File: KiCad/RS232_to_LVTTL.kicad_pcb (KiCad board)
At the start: 2 copper layers, 36.1 x 34 mm, 1 part, among them J1 DB25_Female

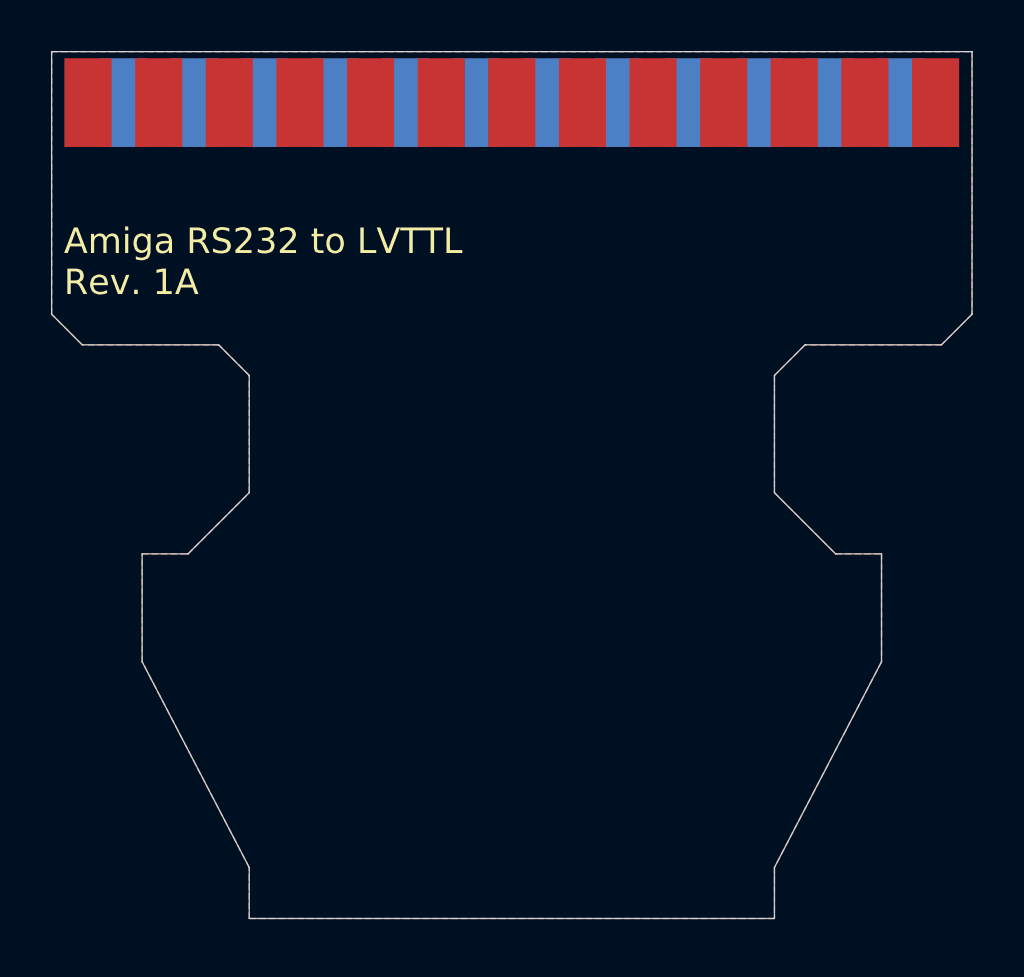
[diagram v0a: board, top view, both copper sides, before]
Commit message: Added power circuit convert 12V to 3.3V
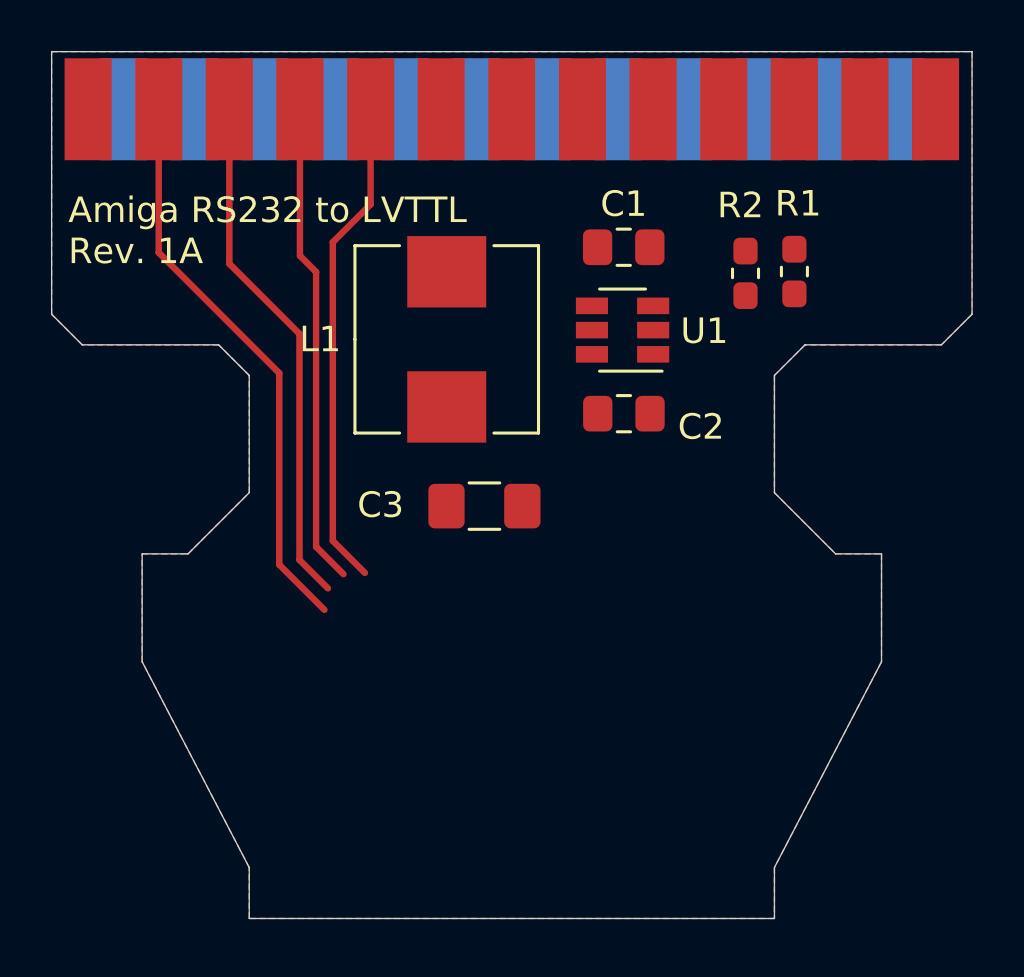
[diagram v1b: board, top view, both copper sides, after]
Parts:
- added C1: 10uF, Capacitor_SMD:C_0805_2012Metric_Pad1.15x1.40mm_HandSolder, F.Cu at (110.9, 57.7)
- added C2: 100nF, Capacitor_SMD:C_0805_2012Metric_Pad1.15x1.40mm_HandSolder, F.Cu at (110.9, 64.2)
- added C3: 47uF, Capacitor_SMD:C_1206_3216Metric_Pad1.42x1.75mm_HandSolder, F.Cu at (105.4, 67.8)
- added L1: L_Small, Inductor_SMD:L_Wuerth_HCM-7050, F.Cu at (103.9, 61.3)
- added R1: 22k, Resistor_SMD:R_0603_1608Metric_Pad1.05x0.95mm_HandSolder, F.Cu at (117.6, 58.6)
- added R2: 100k, Resistor_SMD:R_0603_1608Metric_Pad1.05x0.95mm_HandSolder, F.Cu at (115.7, 58.7)
- added U1: TPS54308, Package_TO_SOT_SMD:SOT-23-6, F.Cu at (110.8, 60.9)
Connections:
- net Net-(J1-Pad2) renamed TXD
- net Net-(J1-Pad3) renamed RXD
- net Net-(J1-Pad4) renamed RTS
- net Net-(J1-Pad5) renamed CTS
- J1 pad 9: Net-(J1-Pad9) -> 12V
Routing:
- net TXD: track 0.00 -> 22.6 mm
- net RXD: track 0.00 -> 20.7 mm
- net CTS: track 0.00 -> 19.6 mm
- net RTS: track 0.00 -> 19.2 mm

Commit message: Added MAX3232 chip
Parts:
- added C4: 100nF, Capacitor_SMD:C_0805_2012Metric_Pad1.15x1.40mm_HandSolder, F.Cu at (115.1, 72.4)
- added U2: MAX3232, Package_SO:TSSOP-16_4.4x5mm_P0.65mm, F.Cu at (106.3, 76.4)
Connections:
- J1 pad 2: TXD -> TX
- J1 pad 3: RXD -> RX
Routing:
- net TXD: track 22.6 -> 0.00 mm
- net TX: track 0.00 -> 22.6 mm
- net RXD: track 20.7 -> 0.00 mm
- net RX: track 0.00 -> 20.7 mm
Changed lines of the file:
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@@
     (tracks 16)
     (zones 0)
-    (modules 8)
-    (nets 31)
+    (modules 10)
+    (nets 41)
   )
   (page A4)
@@
   (net 26 CTS)
   (net 27 RTS)
-  (net 28 RXD)
-  (net 29 TXD)
-  (net 30 3V3)
+  (net 28 3V3)
+  (net 29 "Net-(U2-Pad6)")
+  (net 30 "Net-(U2-Pad5)")
+  (net 31 "Net-(U2-Pad4)")
+  (net 32 "Net-(U2-Pad3)")
+  (net 33 "Net-(U2-Pad2)")
+  (net 34 "Net-(U2-Pad1)")
+  (net 35 RX)
+  (net 36 TX)
+  (net 37 RX_MCU)
+  (net 38 TX_MCU)
+  (net 39 RTS_MCU)
+  (net 40 CTS_MCU)
   (net_class Default "This is the default net class."
     (clearance 0.1524)
@@
     (add_net 3V3)
     (add_net CTS)
+    (add_net CTS_MCU)
     (add_net GND)
     (add_net "Net-(C2-Pad1)")
@@
     (add_net "Net-(R1-Pad1)")
     (add_net "Net-(U1-Pad5)")
+    (add_net "Net-(U2-Pad1)")
+    (add_net "Net-(U2-Pad2)")
+    (add_net "Net-(U2-Pad3)")
+    (add_net "Net-(U2-Pad4)")
+    (add_net "Net-(U2-Pad5)")
+    (add_net "Net-(U2-Pad6)")
     (add_net RTS)
-    (add_net RXD)
-    (add_net TXD)
+    (add_net RTS_MCU)
+    (add_net RX)
+    (add_net RX_MCU)
+    (add_net TX)
+    (add_net TX_MCU)
+  )
+  (module Package_SO:TSSOP-16_4.4x5mm_P0.65mm (layer F.Cu)
+    (at 106.3316 76.39568 180)
+    (descr "16-Lead Plastic Thin Shrink Small Outline (ST)-4.4 mm Body [TSSOP] (see Microchip Packaging Specification 00000049BS.pdf)")
+    (tags "SSOP 0.65")
+    (attr smd)
+    (fp_text reference U2 (at 0 -3.55) (layer F.SilkS)
+      (effects (font (size 1 1) (thickness 0.15)))
+    )
+    (fp_text value MAX3232 (at 0 3.55) (layer F.Fab) hide
+      (effects (font (size 1 1) (thickness 0.15)))
+    )
+    (fp_line (start -3.775 -2.8) (end 2.2 -2.8) (layer F.SilkS) (width 0.15))
+    (fp_line (start -2.2 2.725) (end 2.2 2.725) (layer F.SilkS) (width 0.15))
+    (fp_line (start -3.95 2.8) (end 3.95 2.8) (layer F.CrtYd) (width 0.05))
+    (fp_line (start -3.95 -2.9) (end 3.95 -2.9) (layer F.CrtYd) (width 0.05))
+    (fp_line (start 3.95 -2.9) (end 3.95 2.8) (layer F.CrtYd) (width 0.05))
+    (fp_line (start -3.95 -2.9) (end -3.95 2.8) (layer F.CrtYd) (width 0.05))
+    (fp_line (start -2.2 -1.5) (end -1.2 -2.5) (layer F.Fab) (width 0.15))
+    (fp_line (start -2.2 2.5) (end -2.2 -1.5) (layer F.Fab) (width 0.15))
+    (fp_line (start 2.2 2.5) (end -2.2 2.5) (layer F.Fab) (width 0.15))
+    (fp_line (start 2.2 -2.5) (end 2.2 2.5) (layer F.Fab) (width 0.15))
+    (fp_line (start -1.2 -2.5) (end 2.2 -2.5) (layer F.Fab) (width 0.15))
+    (fp_text user %R (at 0 0) (layer F.Fab) hide
+      (effects (font (size 0.8 0.8) (thickness 0.15)))
+    )
+    (pad 16 smd rect (at 2.95 -2.275 180) (size 1.5 0.45) (layers F.Cu F.Paste F.Mask)
+      (net 28 3V3))
+    (pad 15 smd rect (at 2.95 -1.625 180) (size 1.5 0.45) (layers F.Cu F.Paste F.Mask)
+      (net 1 GND))
+    (pad 14 smd rect (at 2.95 -0.975 180) (size 1.5 0.45) (layers F.Cu F.Paste F.Mask)
+      (net 35 RX))
+    (pad 13 smd rect (at 2.95 -0.325 180) (size 1.5 0.45) (layers F.Cu F.Paste F.Mask)
+      (net 36 TX))
+    (pad 12 smd rect (at 2.95 0.325 180) (size 1.5 0.45) (layers F.Cu F.Paste F.Mask)
+      (net 37 RX_MCU))
+    (pad 11 smd rect (at 2.95 0.975 180) (size 1.5 0.45) (layers F.Cu F.Paste F.Mask)
+      (net 38 TX_MCU))
+    (pad 10 smd rect (at 2.95 1.625 180) (size 1.5 0.45) (layers F.Cu F.Paste F.Mask)
+      (net 39 RTS_MCU))
+    (pad 9 smd rect (at 2.95 2.275 180) (size 1.5 0.45) (layers F.Cu F.Paste F.Mask)
+      (net 40 CTS_MCU))
+    (pad 8 smd rect (at -2.95 2.275 180) (size 1.5 0.45) (layers F.Cu F.Paste F.Mask)
+      (net 27 RTS))
+    (pad 7 smd rect (at -2.95 1.625 180) (size 1.5 0.45) (layers F.Cu F.Paste F.Mask)
+      (net 26 CTS))
+    (pad 6 smd rect (at -2.95 0.975 180) (size 1.5 0.45) (layers F.Cu F.Paste F.Mask)
+      (net 29 "Net-(U2-Pad6)"))
+    (pad 5 smd rect (at -2.95 0.325 180) (size 1.5 0.45) (layers F.Cu F.Paste F.Mask)
+      (net 30 "Net-(U2-Pad5)"))
+    (pad 4 smd rect (at -2.95 -0.325 180) (size 1.5 0.45) (layers F.Cu F.Paste F.Mask)
+      (net 31 "Net-(U2-Pad4)"))
+    (pad 3 smd rect (at -2.95 -0.975 180) (size 1.5 0.45) (layers F.Cu F.Paste F.Mask)
+      (net 32 "Net-(U2-Pad3)"))
+    (pad 2 smd rect (at -2.95 -1.625 180) (size 1.5 0.45) (layers F.Cu F.Paste F.Mask)
+      (net 33 "Net-(U2-Pad2)"))
+    (pad 1 smd rect (at -2.95 -2.275 180) (size 1.5 0.45) (layers F.Cu F.Paste F.Mask)
+      (net 34 "Net-(U2-Pad1)"))
+    (model ${KISYS3DMOD}/Package_SO.3dshapes/TSSOP-16_4.4x5mm_P0.65mm.wrl
+      (at (xyz 0 0 0))
+      (scale (xyz 1 1 1))
+      (rotate (xyz 0 0 0))
+    )
+  )
+  (module Capacitor_SMD:C_0805_2012Metric_Pad1.15x1.40mm_HandSolder (layer F.Cu)
+    (at 115.07174 72.43074)
+    (descr "Capacitor SMD 0805 (2012 Metric), square (rectangular) end terminal, IPC_7351 nominal with elongated pad for handsoldering. (Body size source: https://docs.google.com/spreadsheets/d/1BsfQQcO9C6DZCsRaXUlFlo91Tg2WpOkGARC1WS5S8t0/edit?usp=sharing), generated with kicad-footprint-generator")
+    (tags "capacitor handsolder")
+    (attr smd)
+    (fp_text reference C4 (at 0 -1.65) (layer F.SilkS)
+      (effects (font (size 1 1) (thickness 0.15)))
+    )
+    (fp_text value 100nF (at 0 1.65) (layer F.Fab)
+      (effects (font (size 1 1) (thickness 0.15)))
+    )
+    (fp_line (start 1.85 0.95) (end -1.85 0.95) (layer F.CrtYd) (width 0.05))
+    (fp_line (start 1.85 -0.95) (end 1.85 0.95) (layer F.CrtYd) (width 0.05))
+    (fp_line (start -1.85 -0.95) (end 1.85 -0.95) (layer F.CrtYd) (width 0.05))
+    (fp_line (start -1.85 0.95) (end -1.85 -0.95) (layer F.CrtYd) (width 0.05))
+    (fp_line (start -0.261252 0.71) (end 0.261252 0.71) (layer F.SilkS) (width 0.12))
+    (fp_line (start -0.261252 -0.71) (end 0.261252 -0.71) (layer F.SilkS) (width 0.12))
+    (fp_line (start 1 0.6) (end -1 0.6) (layer F.Fab) (width 0.1))
+    (fp_line (start 1 -0.6) (end 1 0.6) (layer F.Fab) (width 0.1))
+    (fp_line (start -1 -0.6) (end 1 -0.6) (layer F.Fab) (width 0.1))
+    (fp_line (start -1 0.6) (end -1 -0.6) (layer F.Fab) (width 0.1))
+    (fp_text user %R (at 0 0) (layer F.Fab)
+      (effects (font (size 0.5 0.5) (thickness 0.08)))
+    )
+    (pad 2 smd roundrect (at 1.025 0) (size 1.15 1.4) (layers F.Cu F.Paste F.Mask) (roundrect_rratio 0.217391)
+      (net 28 3V3))
+    (pad 1 smd roundrect (at -1.025 0) (size 1.15 1.4) (layers F.Cu F.Paste F.Mask) (roundrect_rratio 0.217391)
+      (net 1 GND))
+    (model ${KISYS3DMOD}/Capacitor_SMD.3dshapes/C_0805_2012Metric.wrl
+      (at (xyz 0 0 0))
+      (scale (xyz 1 1 1))
+      (rotate (xyz 0 0 0))
+    )
   )
   (module Capacitor_SMD:C_1206_3216Metric_Pad1.42x1.75mm_HandSolder (layer F.Cu)
@@
       (net 1 GND))
     (pad 1 smd roundrect (at -1.4875 0) (size 1.425 1.75) (layers F.Cu F.Paste F.Mask) (roundrect_rratio 0.175439)
-      (net 30 3V3))
+      (net 28 3V3))
     (model ${KISYS3DMOD}/Capacitor_SMD.3dshapes/C_1206_3216Metric.wrl
       (at (xyz 0 0 0))
@@
     )
     (pad 2 smd rect (at 2.65 0 270) (size 2.8 3.1) (layers F.Cu F.Paste F.Mask)
-      (net 30 3V3))
+      (net 28 3V3))
     (pad 1 smd rect (at -2.65 0 270) (size 2.8 3.1) (layers F.Cu F.Paste F.Mask)
       (net 24 "Net-(C2-Pad2)"))
@@
       (net 23 "Net-(R1-Pad1)"))
     (pad 1 smd roundrect (at -0.875 0 90) (size 1.05 0.95) (layers F.Cu F.Paste F.Mask) (roundrect_rratio 0.25)
-      (net 30 3V3))
+      (net 28 3V3))
     (model ${KISYS3DMOD}/Resistor_SMD.3dshapes/R_0603_1608Metric.wrl
       (at (xyz 0 0 0))
@@
       (net 27 RTS))
     (pad 3 smd rect (at 11.08 0 180) (size 1.846667 4) (drill (offset 0 -0.26)) (layers F.Cu F.Paste F.Mask)
-      (net 28 RXD))
+      (net 35 RX))
     (pad 2 smd rect (at 13.85 0 180) (size 1.846667 4) (drill (offset 0 -0.26)) (layers F.Cu F.Paste F.Mask)
-      (net 29 TXD))
+      (net 36 TX))
     (pad 1 smd rect (at 16.62 0 180) (size 1.846667 4) (drill (offset 0 -0.26)) (layers F.Cu F.Paste F.Mask)
       (net 7 "Net-(J1-Pad1)"))
@@
   (segment (start 98.82336 58.64108) (end 98.82336 69.42084) (width 0.254) (layer F.Cu) (net 27))
   (segment (start 98.82336 69.42084) (end 99.89778 70.49526) (width 0.254) (layer F.Cu) (net 27))
-  (segment (start 95.42 52) (end 95.42 58.31874) (width 0.254) (layer F.Cu) (net 28))
-  (segment (start 95.42 58.31874) (end 98.17058 61.06932) (width 0.254) (layer F.Cu) (net 28))
-  (segment (start 98.17058 61.06932) (end 98.17058 69.93392) (width 0.254) (layer F.Cu) (net 28))
-  (segment (start 98.17058 69.93392) (end 99.29072 71.05406) (width 0.254) (layer F.Cu) (net 28))
-  (segment (start 92.65 52) (end 92.65 57.88046) (width 0.254) (layer F.Cu) (net 29))
-  (segment (start 92.65 57.88046) (end 97.3781 62.60856) (width 0.254) (layer F.Cu) (net 29))
-  (segment (start 97.3781 62.60856) (end 97.3781 70.12188) (width 0.254) (layer F.Cu) (net 29))
-  (segment (start 97.3781 70.12188) (end 99.15102 71.8948) (width 0.254) (layer F.Cu) (net 29))
+  (segment (start 95.42 52) (end 95.42 58.31874) (width 0.254) (layer F.Cu) (net 35))
+  (segment (start 95.42 58.31874) (end 98.17058 61.06932) (width 0.254) (layer F.Cu) (net 35))
+  (segment (start 98.17058 61.06932) (end 98.17058 69.93392) (width 0.254) (layer F.Cu) (net 35))
+  (segment (start 98.17058 69.93392) (end 99.29072 71.05406) (width 0.254) (layer F.Cu) (net 35))
+  (segment (start 92.65 52) (end 92.65 57.88046) (width 0.254) (layer F.Cu) (net 36))
+  (segment (start 92.65 57.88046) (end 97.3781 62.60856) (width 0.254) (layer F.Cu) (net 36))
+  (segment (start 97.3781 62.60856) (end 97.3781 70.12188) (width 0.254) (layer F.Cu) (net 36))
+  (segment (start 97.3781 70.12188) (end 99.15102 71.8948) (width 0.254) (layer F.Cu) (net 36))
   (zone (net 1) (net_name GND) (layer B.Cu) (hatch edge 0.508)
     (connect_pads (clearance 0.1524))
